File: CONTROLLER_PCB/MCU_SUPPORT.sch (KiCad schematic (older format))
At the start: 32 parts

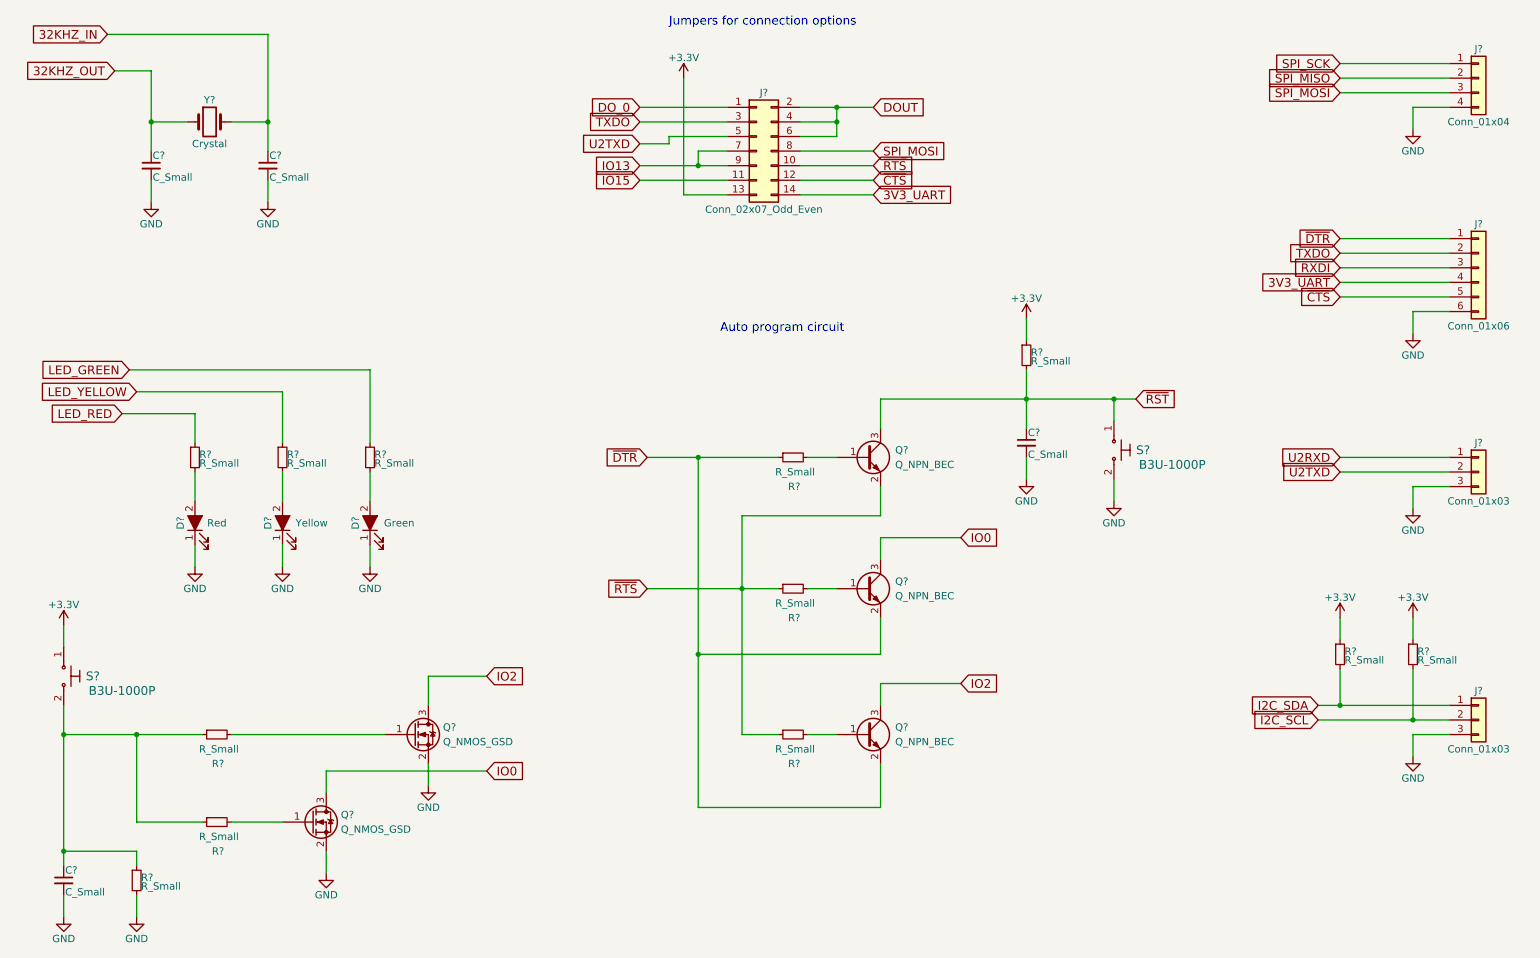
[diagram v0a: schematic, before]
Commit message: Added input filtering, and assigned footprints to most components, several remain.
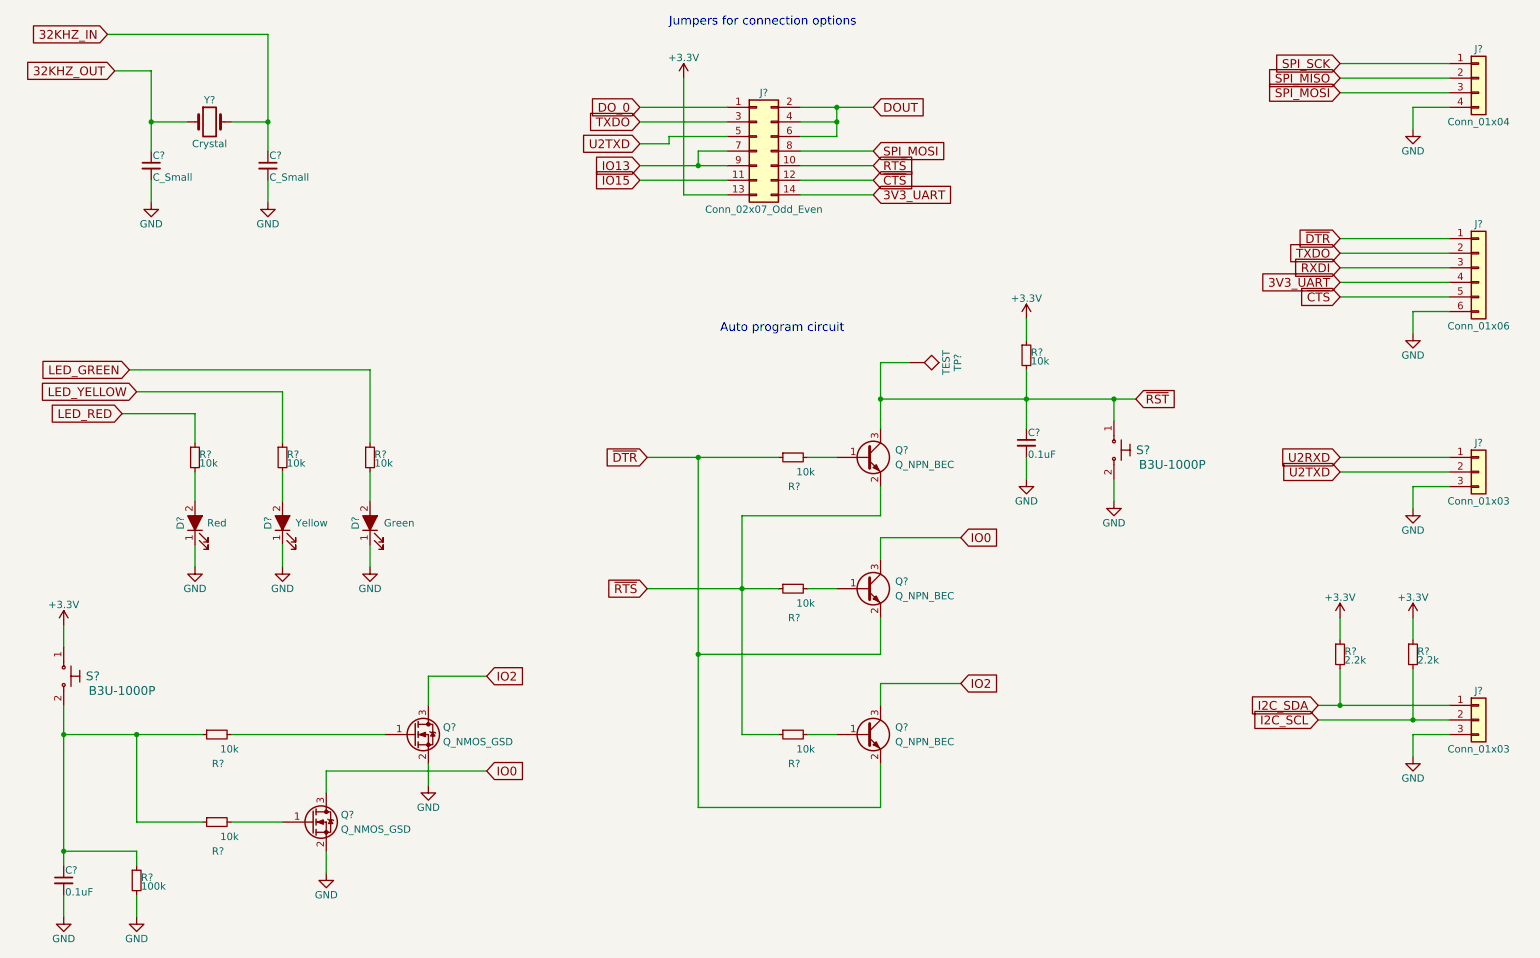
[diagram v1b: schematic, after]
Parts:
- removed C?: C_Small, symbol C_Small
- removed R? (x7): R_Small, symbol R_Small
- added C?: 0.1uF, Capacitors_SMD:C_0603_HandSoldering, symbol C_Small
- added R? (x7): 10k, Resistors_SMD:R_0603_HandSoldering, symbol R_Small
- added TP?: TEST, Measurement_Points:Measurement_Point_Round-SMD-Pad_Small, symbol TEST
- C? (x2): footprint (none) -> Capacitors_SMD:C_0603_HandSoldering
- C?: value C_Small -> 0.1uF; footprint (none) -> Capacitors_SMD:C_0603_HandSoldering
- D? (x3): footprint (none) -> LEDs:LED_0603_HandSoldering
- J?: footprint (none) -> Pin_Headers:Pin_Header_Straight_1x04_Pitch2.54mm_SMD_Pin1Left
- J? (x2): footprint (none) -> Pin_Headers:Pin_Header_Straight_1x03_Pitch2.54mm_SMD_Pin1Left
- J?: footprint (none) -> Pin_Headers:Pin_Header_Straight_1x06_Pitch2.54mm_SMD_Pin1Left
- J?: footprint (none) -> Pin_Headers:Pin_Header_Straight_2x07_Pitch2.54mm_SMD
- Q? (x5): footprint (none) -> TO_SOT_Packages_SMD:SOT-23
- R? (x2): value R_Small -> 2.2k; footprint (none) -> Resistors_SMD:R_0603_HandSoldering
- R? (x2): value R_Small -> 10k; footprint (none) -> Resistors_SMD:R_0603_HandSoldering
- R?: value R_Small -> 100k; footprint (none) -> Resistors_SMD:R_0603_HandSoldering
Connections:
- net +3V3: now also R?.1
- net GND: now also C?.2
- net LED_GREEN: now also R?.1
- net LED_YELLOW: now also R?.1
- net ~RST: now also C?.1, R?.2, TP?.1
- net ~RTS: now also R?.1, R?.1
- net at Q?.1 (B): now also R?.2 (x2)
- net at C?.1, R?.1, S?.2: now also R?.1, R?.1
- net at Q?.1 (G): now also R?.2 (x2)
- net at D?.2 (A): now also R?.2 (x2)

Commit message: Finalized schematic, created BOM, started placement (no PCB size yet)
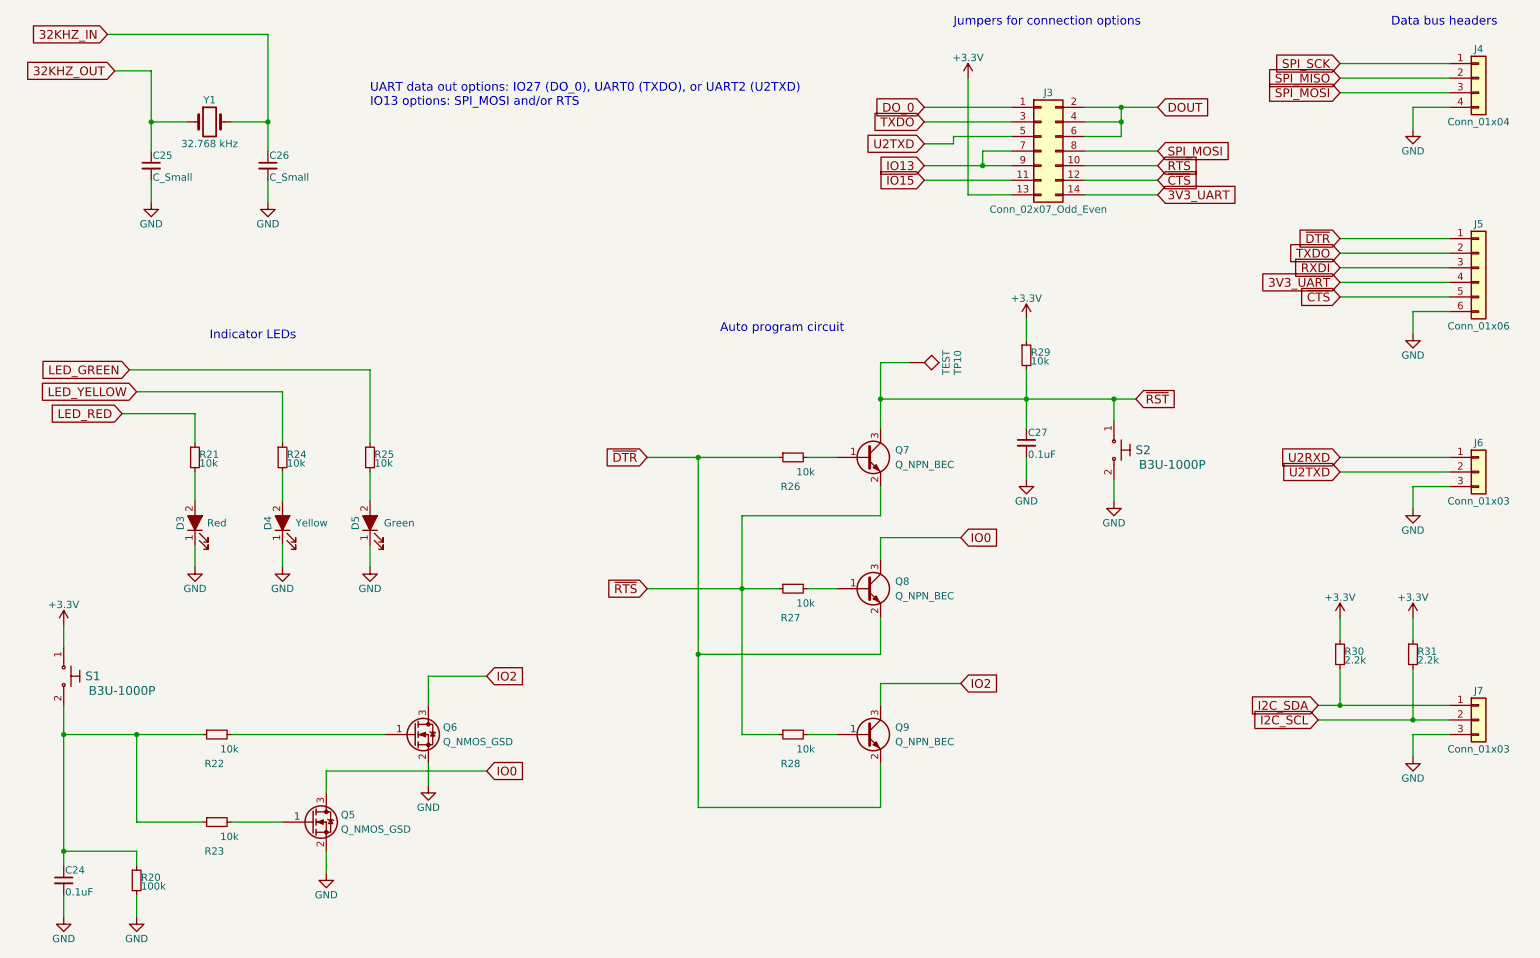
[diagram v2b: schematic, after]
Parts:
- Y1: renamed from Y?; value Crystal -> 32.768 kHz; footprint (none) -> Crystals:Crystal_SMD_3215-2pin_3.2x1.5mm; P/N (none) -> FC-135 32.7680KA-A0
- gave numbers to parts that had none: 32
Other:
- note added: "Data bus headers"
- note added: "Indicator LEDs"
- note added: "UART data out options: IO27 (DO_0), UART0 (TXDO), or UART2 (U2TXD)\nIO13 options: SPI_MOSI and/or RTS"
- moved on the sheet: J3
